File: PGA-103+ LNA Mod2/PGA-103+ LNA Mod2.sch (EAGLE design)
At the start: 44 parts, among them IC1 7805DT, K1 G2RE, K2 G2RE, K3 G2RE, K4 G2RE, X1 SMA, X2 SMA

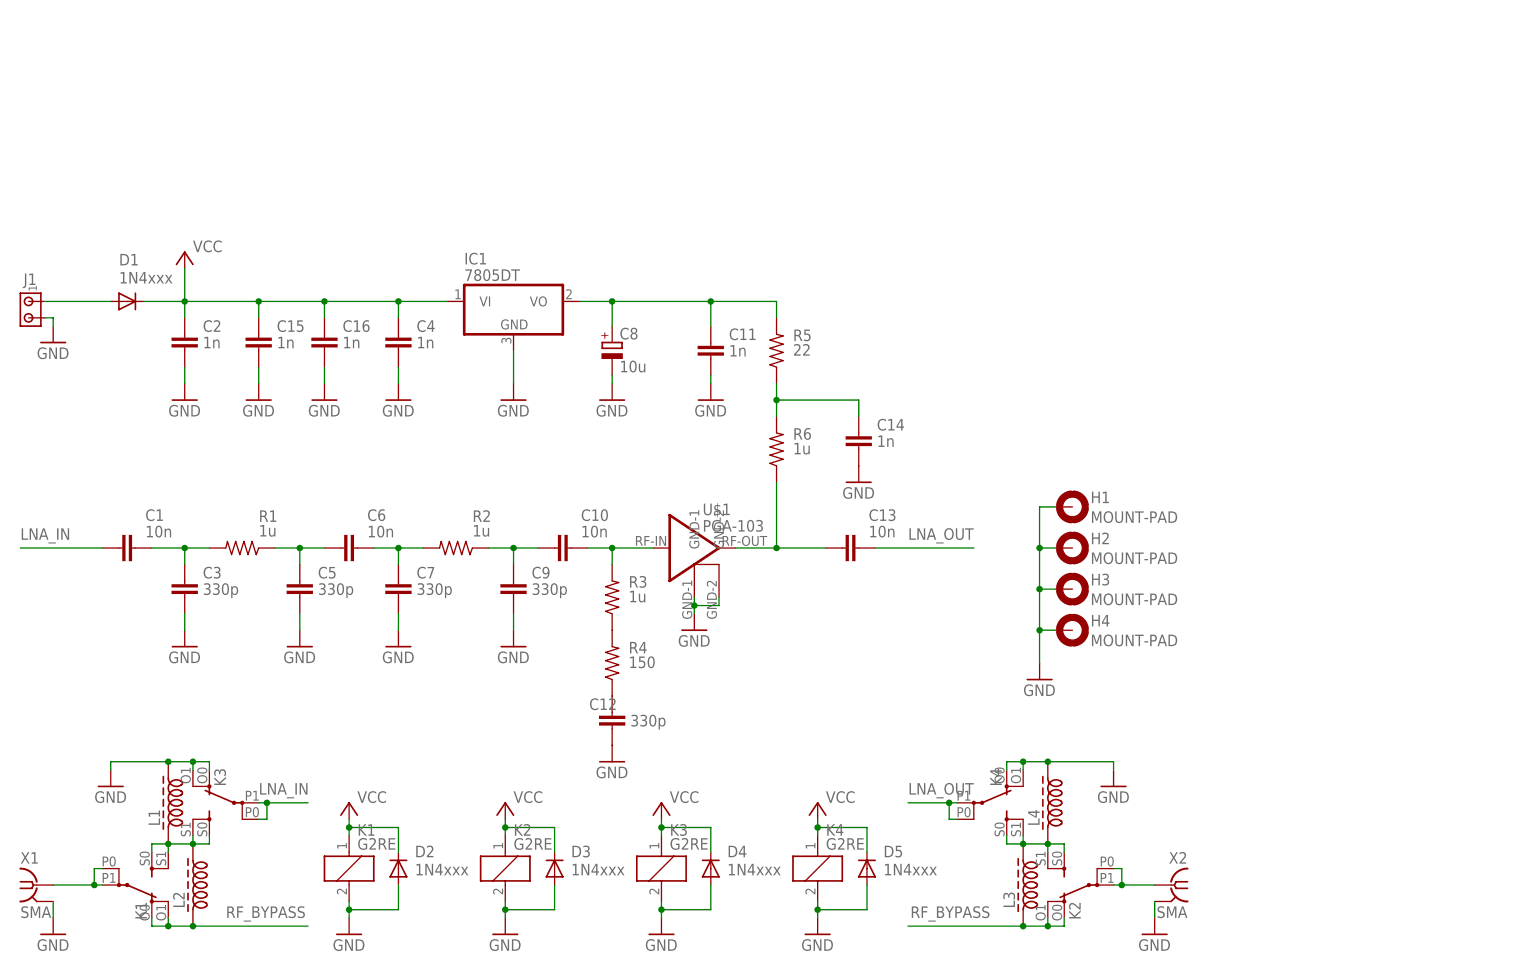
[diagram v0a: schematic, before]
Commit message: Adding partlist and sch.pdf
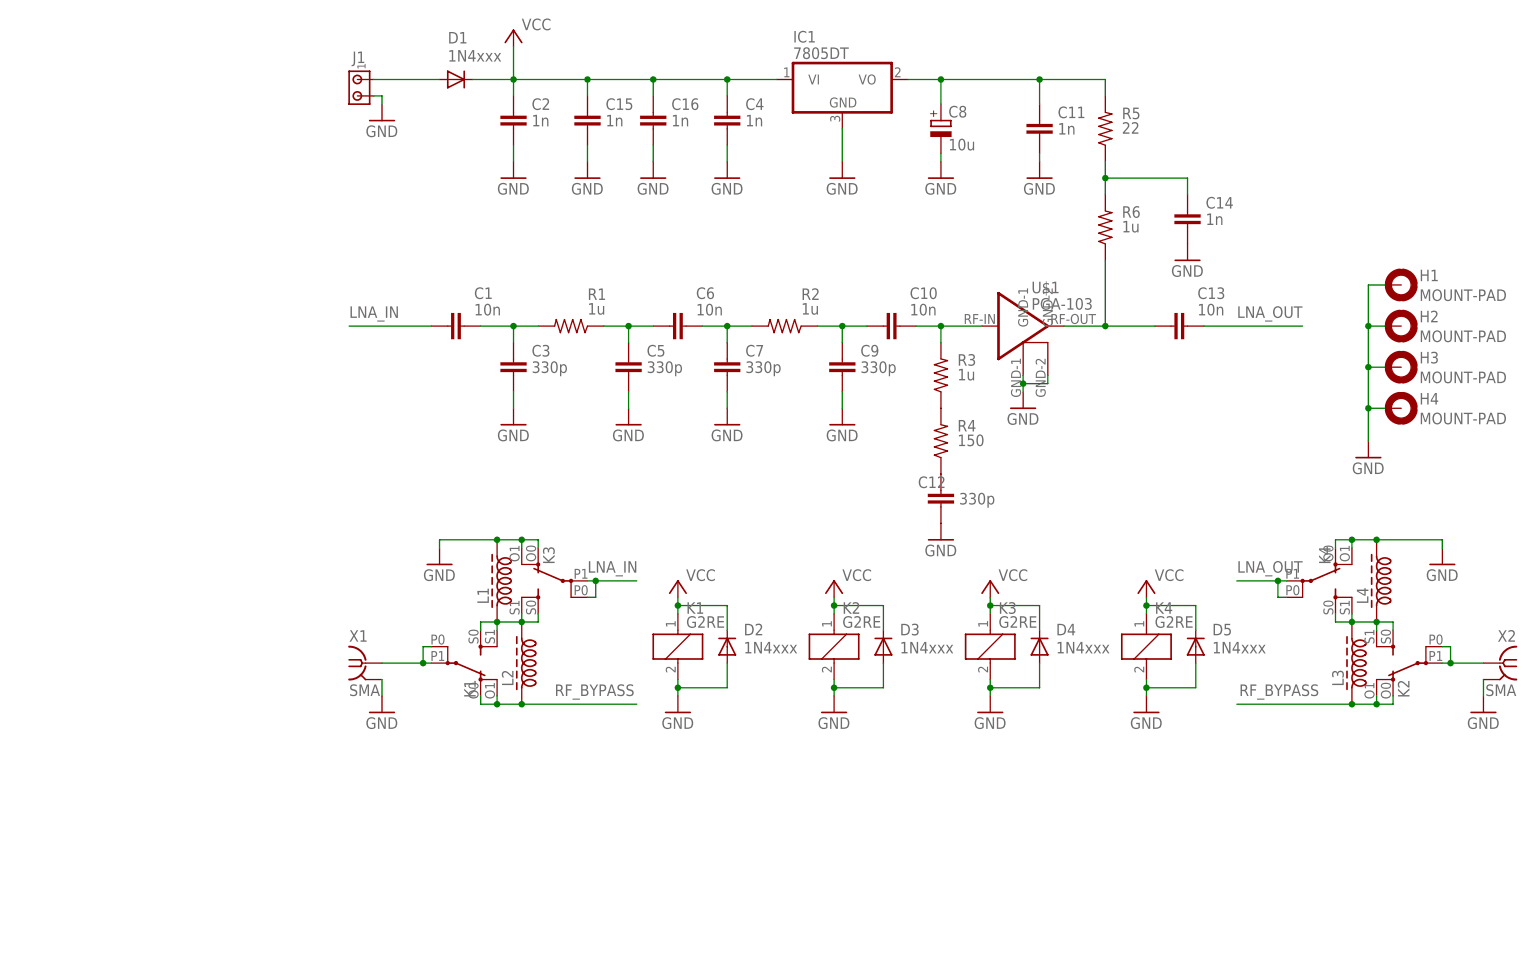
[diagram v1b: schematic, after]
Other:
- moved on the sheet: C1, C10, C11, C12, C13, C14, C15, C16, C2, C3, C4, C5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

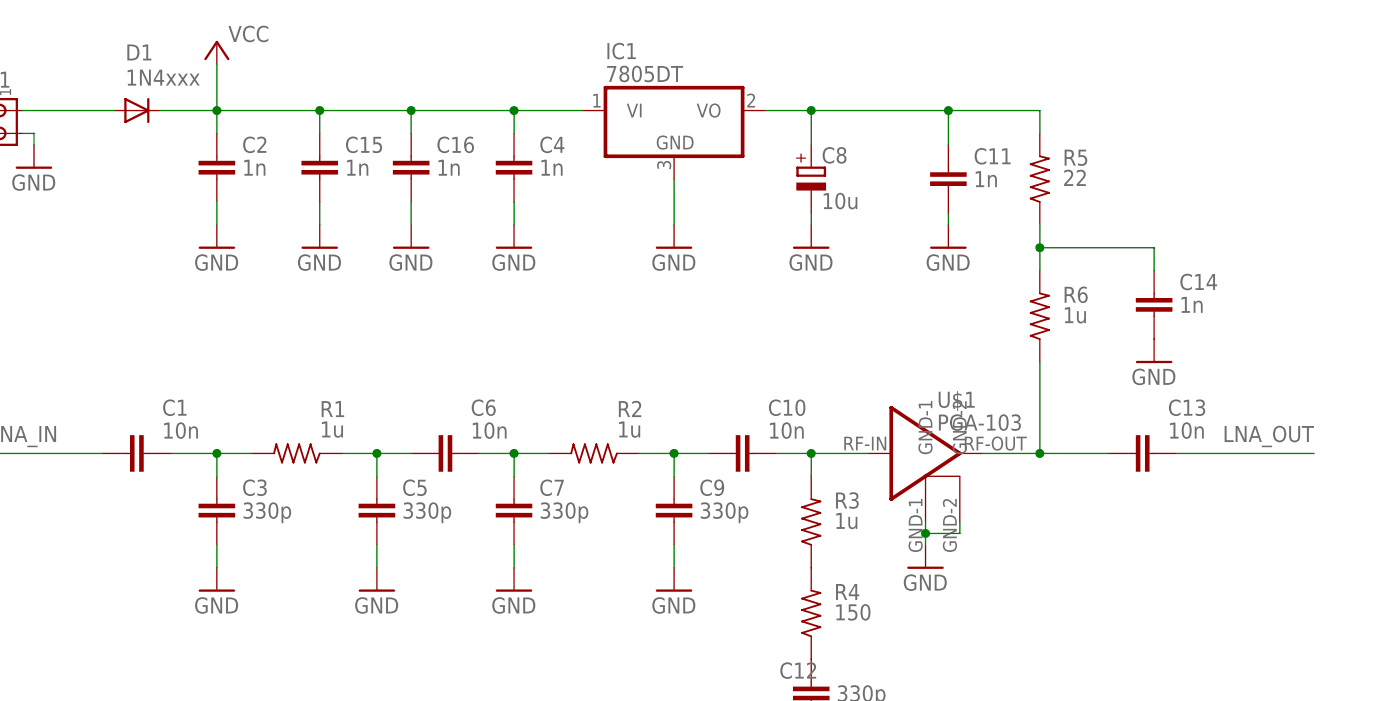
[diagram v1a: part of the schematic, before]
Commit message: Revalue the components
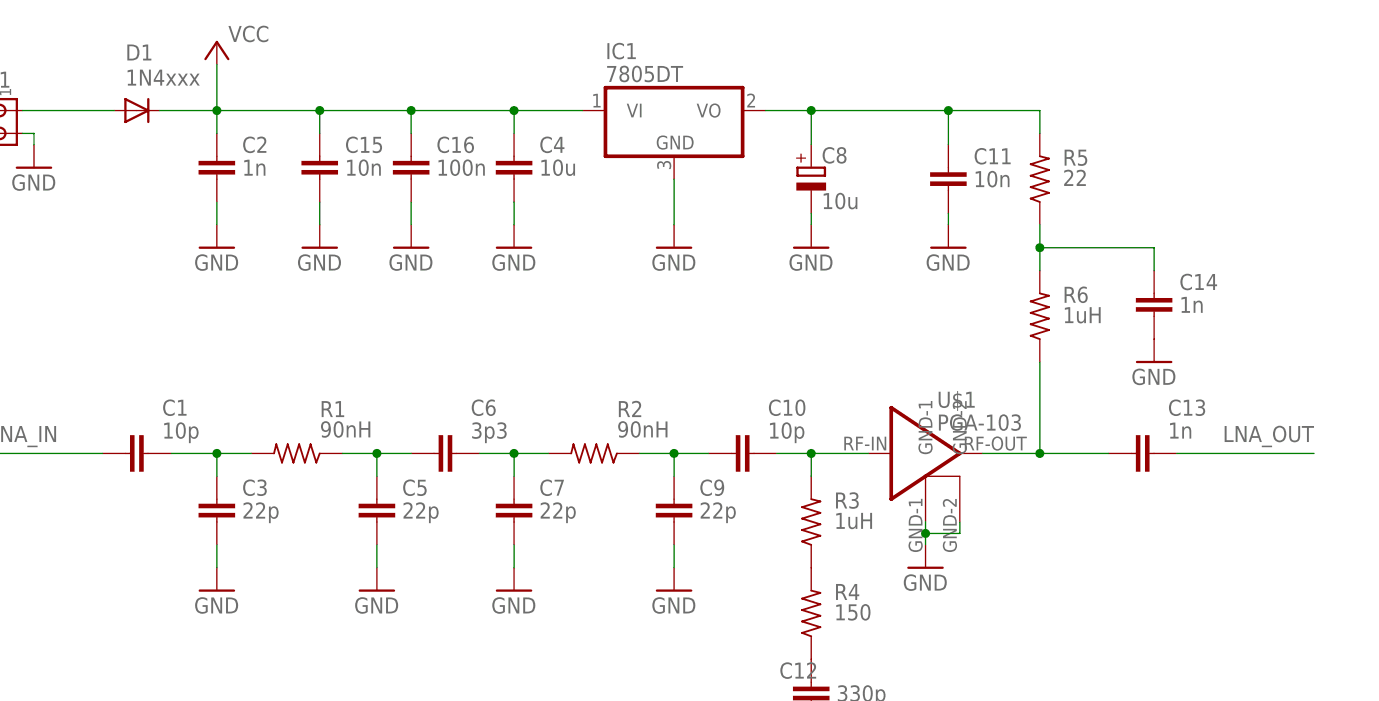
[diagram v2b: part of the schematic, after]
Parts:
- C1, C10: value 10n -> 10p
- C11, C15: value 1n -> 10n
- C13: value 10n -> 1n
- C16: value 1n -> 100n
- C3, C5, C7, C9: value 330p -> 22p
- C4: value 1n -> 10u
- C6: value 10n -> 3p3
- R1, R2: value 1u -> 90nH
- R3, R6: value 1u -> 1uH
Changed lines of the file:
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@@
 <setting verticaltext="up"/>
 </settings>
-<grid distance="1.27" unitdist="mm" unit="mm" style="dots" multiple="1" display="yes" altdistance="0.01" altunitdist="inch" altunit="inch"/>
+<grid distance="0.1" unitdist="inch" unit="inch" style="lines" multiple="1" display="no" altdistance="0.01" altunitdist="inch" altunit="inch"/>
 <layers>
 <layer number="1" name="Top" color="4" fill="1" visible="no" active="no"/>
@@
 </classes>
 <parts>
-<part name="R3" library="rcl" deviceset="R-US_" device="M1206" value="1u"/>
+<part name="R3" library="rcl" deviceset="R-US_" device="M1206" value="1uH"/>
 <part name="R4" library="rcl" deviceset="R-US_" device="M1206" value="150"/>
-<part name="C10" library="rcl" deviceset="C-EU" device="C1206" value="10n"/>
-<part name="C13" library="rcl" deviceset="C-EU" device="C1206" value="10n"/>
+<part name="C10" library="rcl" deviceset="C-EU" device="C1206" value="10p"/>
+<part name="C13" library="rcl" deviceset="C-EU" device="C1206" value="1n"/>
 <part name="C12" library="rcl" deviceset="C-EU" device="C1206" value="330p"/>
-<part name="C11" library="rcl" deviceset="C-EU" device="C1206" value="1n"/>
+<part name="C11" library="rcl" deviceset="C-EU" device="C1206" value="10n"/>
 <part name="C14" library="rcl" deviceset="C-EU" device="C1206" value="1n"/>
 <part name="GND17" library="supply1" deviceset="GND" device=""/>
@@
 <part name="GND12" library="supply1" deviceset="GND" device=""/>
 <part name="GND14" library="supply1" deviceset="GND" device=""/>
-<part name="R6" library="rcl" deviceset="R-US_" device="M1206" value="1u"/>
+<part name="R6" library="rcl" deviceset="R-US_" device="M1206" value="1uH"/>
 <part name="R5" library="rcl" deviceset="R-US_" device="M1206" value="22"/>
 <part name="GND19" library="supply1" deviceset="GND" device=""/>
@@
 <part name="GND2" library="supply1" deviceset="GND" device=""/>
 <part name="X1" library="con-coax" deviceset="SMA-" device="142-0701-851/861" value="SMA"/>
-<part name="C4" library="rcl" deviceset="C-EU" device="C1206" value="1n"/>
+<part name="C4" library="rcl" deviceset="C-EU" device="C1206" value="10u"/>
 <part name="C2" library="rcl" deviceset="C-EU" device="C1206" value="1n"/>
 <part name="GND4" library="supply1" deviceset="GND" device=""/>
 <part name="IC1" library="linear" deviceset="78*" device="DT" technology="05"/>
-<part name="C1" library="rcl" deviceset="C-EU" device="C1206" value="10n"/>
-<part name="R1" library="rcl" deviceset="R-US_" device="M1206" value="1u"/>
-<part name="C6" library="rcl" deviceset="C-EU" device="C1206" value="10n"/>
-<part name="R2" library="rcl" deviceset="R-US_" device="M1206" value="1u"/>
-<part name="C9" library="rcl" deviceset="C-EU" device="C1206" value="330p"/>
-<part name="C7" library="rcl" deviceset="C-EU" device="C1206" value="330p"/>
-<part name="C5" library="rcl" deviceset="C-EU" device="C1206" value="330p"/>
-<part name="C3" library="rcl" deviceset="C-EU" device="C1206" value="330p"/>
+<part name="C1" library="rcl" deviceset="C-EU" device="C1206" value="10p"/>
+<part name="R1" library="rcl" deviceset="R-US_" device="M1206" value="90nH"/>
+<part name="C6" library="rcl" deviceset="C-EU" device="C1206" value="3p3"/>
+<part name="R2" library="rcl" deviceset="R-US_" device="M1206" value="90nH"/>
+<part name="C9" library="rcl" deviceset="C-EU" device="C1206" value="22p"/>
+<part name="C7" library="rcl" deviceset="C-EU" device="C1206" value="22p"/>
+<part name="C5" library="rcl" deviceset="C-EU" device="C1206" value="22p"/>
+<part name="C3" library="rcl" deviceset="C-EU" device="C1206" value="22p"/>
 <part name="GND13" library="supply1" deviceset="GND" device=""/>
 <part name="GND10" library="supply1" deviceset="GND" device=""/>
@@
 <part name="U$1" library="minicircuits" deviceset="PGA-103" device=""/>
 <part name="GND23" library="supply1" deviceset="GND" device=""/>
-<part name="C15" library="rcl" deviceset="C-EU" device="C1206" value="1n"/>
+<part name="C15" library="rcl" deviceset="C-EU" device="C1206" value="10n"/>
 <part name="GND24" library="supply1" deviceset="GND" device=""/>
-<part name="C16" library="rcl" deviceset="C-EU" device="C1206" value="1n"/>
+<part name="C16" library="rcl" deviceset="C-EU" device="C1206" value="100n"/>
 <part name="FRAME1" library="frames" deviceset="A4L-LOC" device=""/>
 </parts>
